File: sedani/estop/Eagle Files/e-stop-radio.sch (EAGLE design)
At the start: 31 parts, among them J1 E-STOP HEADER, J2 AVR_SPI_PROG_3X2PTH, J3 Buttons, J4 5-1814832-1, U1 RFM69HCW, U2 TPS62203DBVR, U3 CD40109BPWR

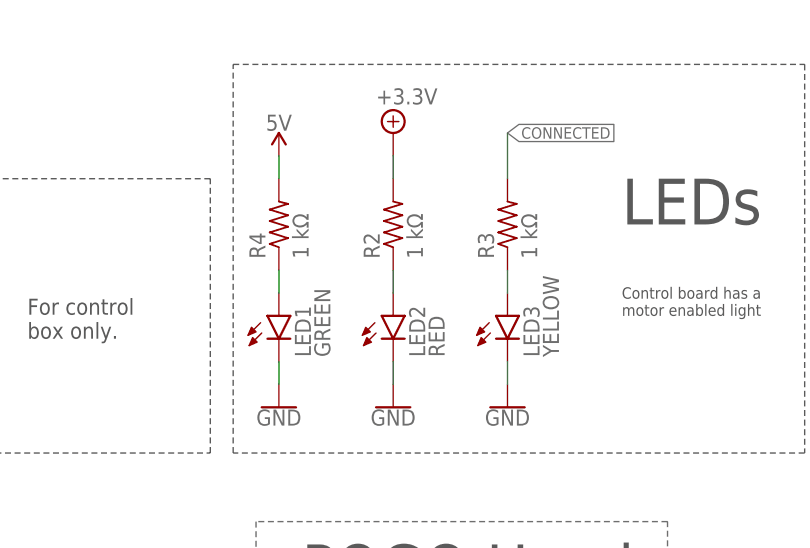
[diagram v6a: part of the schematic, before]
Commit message: fixed silkscreen and almost done routing
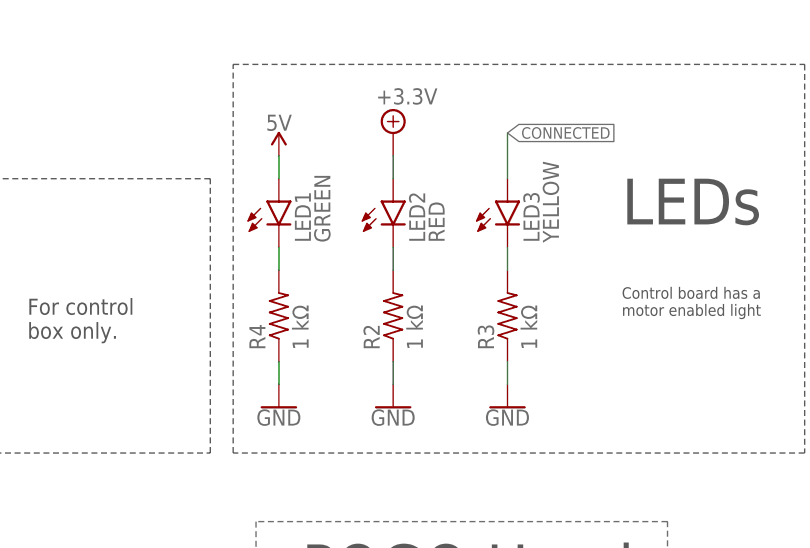
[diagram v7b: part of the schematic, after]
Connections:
- net +3.3V: now also LED2.A; no longer R2.2
- net 5V: now also LED1.A; no longer R4.2
- net CONNECTED: now also LED3.A; no longer R3.2
- net GND: now also R2.1, R3.1, R4.1; no longer LED1.C, LED2.C, LED3.C
- net N$2: now also LED3.C, R3.2; no longer LED2.A, R2.1
- net N$3: now also LED1.C, R4.2; no longer LED1.A, R4.1
- net N$4: now also LED2.C, R2.2; no longer LED3.A, R3.1
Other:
- moved on the sheet: LED1, LED2, LED3, R2, R3, R4
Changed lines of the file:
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@@
 <part name="GND4" library="SparkFun-PowerSymbols" deviceset="GND" device=""/>
 <part name="LED1" library="led" library_urn="urn:adsk.eagle:library:259" deviceset="LED" device="CHIP-LED0603" package3d_urn="urn:adsk.eagle:package:15819/3" value="GREEN"/>
-<part name="R4" library="rcl" library_urn="urn:adsk.eagle:library:334" deviceset="R-US_" device="R0603" package3d_urn="urn:adsk.eagle:package:23555/3" value="1 kΩ"/>
 <part name="GND5" library="SparkFun-PowerSymbols" deviceset="GND" device=""/>
 <part name="LED2" library="led" library_urn="urn:adsk.eagle:library:259" deviceset="LED" device="CHIP-LED0603" package3d_urn="urn:adsk.eagle:package:15819/3" value="RED"/>
-<part name="R2" library="rcl" library_urn="urn:adsk.eagle:library:334" deviceset="R-US_" device="R0603" package3d_urn="urn:adsk.eagle:package:23555/3" value="1 kΩ"/>
 <part name="GND6" library="SparkFun-PowerSymbols" deviceset="GND" device=""/>
 <part name="LED3" library="led" library_urn="urn:adsk.eagle:library:259" deviceset="LED" device="CHIP-LED0603" package3d_urn="urn:adsk.eagle:package:15819/3" value="YELLOW"/>
-<part name="R3" library="rcl" library_urn="urn:adsk.eagle:library:334" deviceset="R-US_" device="R0603" package3d_urn="urn:adsk.eagle:package:23555/3" value="1 kΩ"/>
 <part name="GND7" library="SparkFun-PowerSymbols" deviceset="GND" device=""/>
 <part name="SUPPLY13" library="SparkFun-PowerSymbols" deviceset="5V" device=""/>
@@
 <part name="J4" library="estop-v1.0" deviceset="5-1814832-1" device=""/>
 <part name="SUPPLY20" library="supply2" library_urn="urn:adsk.eagle:library:372" deviceset="GND" device=""/>
+<part name="R4" library="rcl" library_urn="urn:adsk.eagle:library:334" deviceset="R-US_" device="R0603" package3d_urn="urn:adsk.eagle:package:23555/3" value="1 kΩ"/>
+<part name="R2" library="rcl" library_urn="urn:adsk.eagle:library:334" deviceset="R-US_" device="R0603" package3d_urn="urn:adsk.eagle:package:23555/3" value="1 kΩ"/>
+<part name="R3" library="rcl" library_urn="urn:adsk.eagle:library:334" deviceset="R-US_" device="R0603" package3d_urn="urn:adsk.eagle:package:23555/3" value="1 kΩ"/>
 </parts>
 <sheets>
@@
 <attribute name="VALUE" x="243.84" y="-33.274" size="1.778" layer="96" align="top-center"/>
 </instance>
-<instance part="LED1" gate="G$1" x="299.72" y="78.74" smashed="yes">
-<attribute name="NAME" x="303.276" y="74.168" size="1.778" layer="95" rot="R90"/>
-<attribute name="VALUE" x="305.435" y="74.168" size="1.778" layer="96" rot="R90"/>
-</instance>
-<instance part="R4" gate="G$1" x="299.72" y="88.9" smashed="yes" rot="R90">
-<attribute name="NAME" x="298.2214" y="85.09" size="1.778" layer="95" rot="R90"/>
-<attribute name="VALUE" x="303.022" y="85.09" size="1.778" layer="96" rot="R90"/>
+<instance part="LED1" gate="G$1" x="299.72" y="91.44" smashed="yes">
+<attribute name="NAME" x="303.276" y="86.868" size="1.778" layer="95" rot="R90"/>
+<attribute name="VALUE" x="305.435" y="86.868" size="1.778" layer="96" rot="R90"/>
 </instance>
 <instance part="GND5" gate="1" x="299.72" y="68.58" smashed="yes">
 <attribute name="VALUE" x="299.72" y="68.326" size="1.778" layer="96" align="top-center"/>
 </instance>
-<instance part="LED2" gate="G$1" x="312.42" y="78.74" smashed="yes">
-<attribute name="NAME" x="315.976" y="74.168" size="1.778" layer="95" rot="R90"/>
-<attribute name="VALUE" x="318.135" y="74.168" size="1.778" layer="96" rot="R90"/>
-</instance>
-<instance part="R2" gate="G$1" x="312.42" y="88.9" smashed="yes" rot="R90">
-<attribute name="NAME" x="310.9214" y="85.09" size="1.778" layer="95" rot="R90"/>
-<attribute name="VALUE" x="315.722" y="85.09" size="1.778" layer="96" rot="R90"/>
+<instance part="LED2" gate="G$1" x="312.42" y="91.44" smashed="yes">
+<attribute name="NAME" x="315.976" y="86.868" size="1.778" layer="95" rot="R90"/>
+<attribute name="VALUE" x="318.135" y="86.868" size="1.778" layer="96" rot="R90"/>
 </instance>
 <instance part="GND6" gate="1" x="312.42" y="68.58" smashed="yes">
 <attribute name="VALUE" x="312.42" y="68.326" size="1.778" layer="96" align="top-center"/>
 </instance>
-<instance part="LED3" gate="G$1" x="325.12" y="78.74" smashed="yes">
-<attribute name="NAME" x="328.676" y="74.168" size="1.778" layer="95" rot="R90"/>
-<attribute name="VALUE" x="330.835" y="74.168" size="1.778" layer="96" rot="R90"/>
-</instance>
-<instance part="R3" gate="G$1" x="325.12" y="88.9" smashed="yes" rot="R90">
-<attribute name="NAME" x="323.6214" y="85.09" size="1.778" layer="95" rot="R90"/>
-<attribute name="VALUE" x="328.422" y="85.09" size="1.778" layer="96" rot="R90"/>
+<instance part="LED3" gate="G$1" x="325.12" y="91.44" smashed="yes">
+<attribute name="NAME" x="328.676" y="86.868" size="1.778" layer="95" rot="R90"/>
+<attribute name="VALUE" x="330.835" y="86.868" size="1.778" layer="96" rot="R90"/>
 </instance>
 <instance part="GND7" gate="1" x="325.12" y="68.58" smashed="yes">
@@
 <instance part="SUPPLY20" gate="GND" x="327.66" y="-35.56" smashed="yes">
 <attribute name="VALUE" x="325.755" y="-38.735" size="1.778" layer="96"/>
+</instance>
+<instance part="R4" gate="G$1" x="299.72" y="78.74" smashed="yes" rot="R90">
+<attribute name="NAME" x="298.2214" y="74.93" size="1.778" layer="95" rot="R90"/>
+<attribute name="VALUE" x="303.022" y="74.93" size="1.778" layer="96" rot="R90"/>
+</instance>
+<instance part="R2" gate="G$1" x="312.42" y="78.74" smashed="yes" rot="R90">
+<attribute name="NAME" x="310.9214" y="74.93" size="1.778" layer="95" rot="R90"/>
+<attribute name="VALUE" x="315.722" y="74.93" size="1.778" layer="96" rot="R90"/>
+</instance>
+<instance part="R3" gate="G$1" x="325.12" y="78.74" smashed="yes" rot="R90">
+<attribute name="NAME" x="323.6214" y="74.93" size="1.778" layer="95" rot="R90"/>
+<attribute name="VALUE" x="328.422" y="74.93" size="1.778" layer="96" rot="R90"/>
 </instance>
 </instances>
@@
 </segment>
 <segment>
-<pinref part="GND6" gate="1" pin="GND"/>
-<pinref part="LED2" gate="G$1" pin="C"/>
-<wire x1="312.42" y1="71.12" x2="312.42" y2="73.66" width="0.1524" layer="91"/>
-</segment>
-<segment>
-<pinref part="GND7" gate="1" pin="GND"/>
-<pinref part="LED3" gate="G$1" pin="C"/>
-<wire x1="325.12" y1="71.12" x2="325.12" y2="73.66" width="0.1524" layer="91"/>
-</segment>
-<segment>
-<pinref part="GND5" gate="1" pin="GND"/>
-<pinref part="LED1" gate="G$1" pin="C"/>
-<wire x1="299.72" y1="71.12" x2="299.72" y2="73.66" width="0.1524" layer="91"/>
-</segment>
-<segment>
 <pinref part="J1" gate="G$1" pin="7"/>
 <pinref part="GND" gate="1" pin="GND"/>
@@
 <pinref part="SUPPLY20" gate="GND" pin="GND"/>
 <wire x1="332.74" y1="-33.02" x2="327.66" y2="-33.02" width="0.1524" layer="91"/>
+</segment>
+<segment>
+<pinref part="R4" gate="G$1" pin="1"/>
+<pinref part="GND5" gate="1" pin="GND"/>
+<wire x1="299.72" y1="73.66" x2="299.72" y2="71.12" width="0.1524" layer="91"/>
+</segment>
+<segment>
+<pinref part="GND6" gate="1" pin="GND"/>
+<pinref part="R2" gate="G$1" pin="1"/>
+<wire x1="312.42" y1="71.12" x2="312.42" y2="73.66" width="0.1524" layer="91"/>
+</segment>
+<segment>
+<pinref part="R3" gate="G$1" pin="1"/>
+<pinref part="GND7" gate="1" pin="GND"/>
+<wire x1="325.12" y1="73.66" x2="325.12" y2="71.12" width="0.1524" layer="91"/>
 </segment>
 </net>
@@
 </segment>
 <segment>
-<pinref part="R2" gate="G$1" pin="2"/>
-<pinref part="SUPPLY14" gate="P" pin="+3.3V"/>
-<wire x1="312.42" y1="93.98" x2="312.42" y2="96.52" width="0.1524" layer="91"/>
-</segment>
-<segment>
 <pinref part="U3" gate="A" pin="VCC"/>
 <pinref part="SUPPLY16" gate="P" pin="+3.3V"/>
@@
 <wire x1="246.38" y1="30.48" x2="246.38" y2="27.94" width="0.1524" layer="91"/>
 <wire x1="246.38" y1="27.94" x2="236.22" y2="27.94" width="0.1524" layer="91"/>
+</segment>
+<segment>
+<pinref part="LED2" gate="G$1" pin="A"/>
+<wire x1="312.42" y1="96.52" x2="312.42" y2="93.98" width="0.1524" layer="91"/>
+<pinref part="SUPPLY14" gate="P" pin="+3.3V"/>
 </segment>
 </net>
@@
 </segment>
 <segment>
-<pinref part="R4" gate="G$1" pin="2"/>
 <pinref part="SUPPLY13" gate="G$1" pin="5V"/>
 <wire x1="299.72" y1="93.98" x2="299.72" y2="96.52" width="0.1524" layer="91"/>
+<pinref part="LED1" gate="G$1" pin="A"/>
 </segment>
 <segment>
@@
 </segment>
 </net>
-<net name="N$3" class="0">
-<segment>
-<pinref part="R4" gate="G$1" pin="1"/>
-<pinref part="LED1" gate="G$1" pin="A"/>
-<wire x1="299.72" y1="83.82" x2="299.72" y2="81.28" width="0.1524" layer="91"/>
-</segment>
-</net>
-<net name="N$2" class="0">
-<segment>
-<pinref part="R2" gate="G$1" pin="1"/>
-<pinref part="LED2" gate="G$1" pin="A"/>
-<wire x1="312.42" y1="83.82" x2="312.42" y2="81.28" width="0.1524" layer="91"/>
-</segment>
-</net>
-<net name="N$4" class="0">
-<segment>
-<pinref part="R3" gate="G$1" pin="1"/>
-<pinref part="LED3" gate="G$1" pin="A"/>
-<wire x1="325.12" y1="83.82" x2="325.12" y2="81.28" width="0.1524" layer="91"/>
-</segment>
-</net>
 <net name="N$7" class="1">
 <segment>
@@
 <net name="CONNECTED" class="0">
 <segment>
-<pinref part="R3" gate="G$1" pin="2"/>
 <wire x1="325.12" y1="93.98" x2="325.12" y2="99.06" width="0.1524" layer="91"/>
 <label x="325.12" y="99.06" size="1.27" layer="95" font="vector" xref="yes"/>
+<pinref part="LED3" gate="G$1" pin="A"/>
 </segment>
 <segment>
@@
 </segment>
 </net>
+<net name="N$3" class="0">
+<segment>
+<pinref part="R4" gate="G$1" pin="2"/>
+<pinref part="LED1" gate="G$1" pin="C"/>
+<wire x1="299.72" y1="83.82" x2="299.72" y2="86.36" width="0.1524" layer="91"/>
+</segment>
+</net>
+<net name="N$4" class="0">
+<segment>
+<pinref part="R2" gate="G$1" pin="2"/>
+<pinref part="LED2" gate="G$1" pin="C"/>
+<wire x1="312.42" y1="83.82" x2="312.42" y2="86.36" width="0.1524" layer="91"/>
+</segment>
+</net>
+<net name="N$2" class="0">
+<segment>
+<pinref part="LED3" gate="G$1" pin="C"/>
+<pinref part="R3" gate="G$1" pin="2"/>
+<wire x1="325.12" y1="86.36" x2="325.12" y2="83.82" width="0.1524" layer="91"/>
+</segment>
+</net>

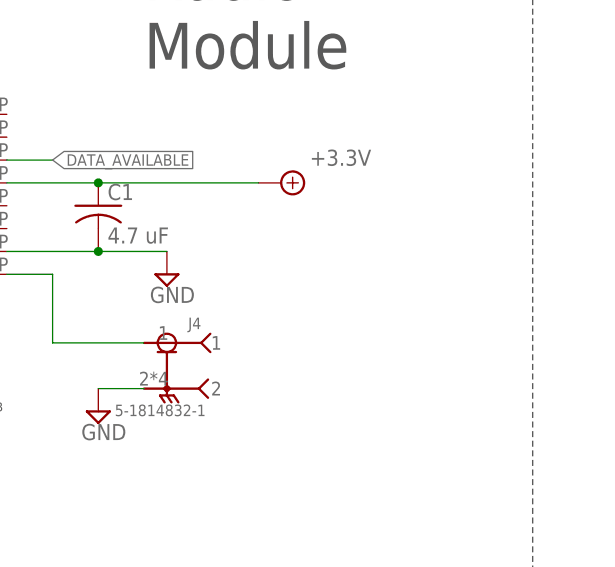
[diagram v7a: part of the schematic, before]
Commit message: added drill holes. Moved voltage regulator
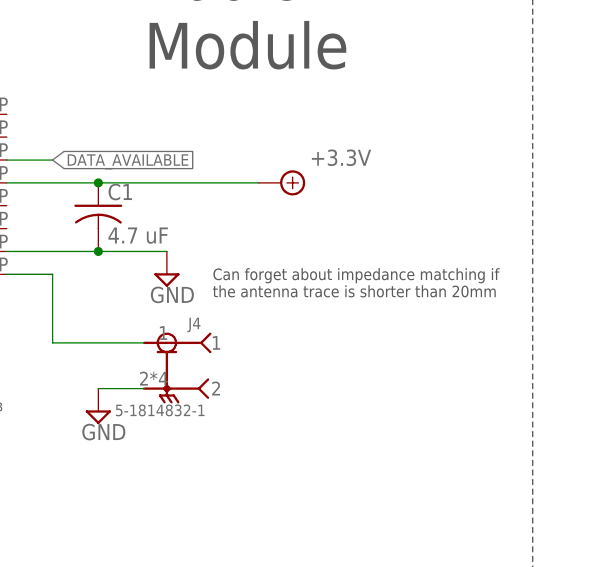
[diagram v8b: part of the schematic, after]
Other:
- note added: "Can forget about impedance matching if the antenna trace is shorter than 20mm"
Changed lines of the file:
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@@
 should be solderbridged on the
 module that goes in Sedani.</text>
+<text x="340.36" y="-22.86" size="1.27" layer="97" font="vector">Can forget about impedance matching if
+the antenna trace is shorter than 20mm</text>
 </plain>
 <instances>
